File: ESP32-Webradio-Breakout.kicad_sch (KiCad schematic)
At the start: 6 parts

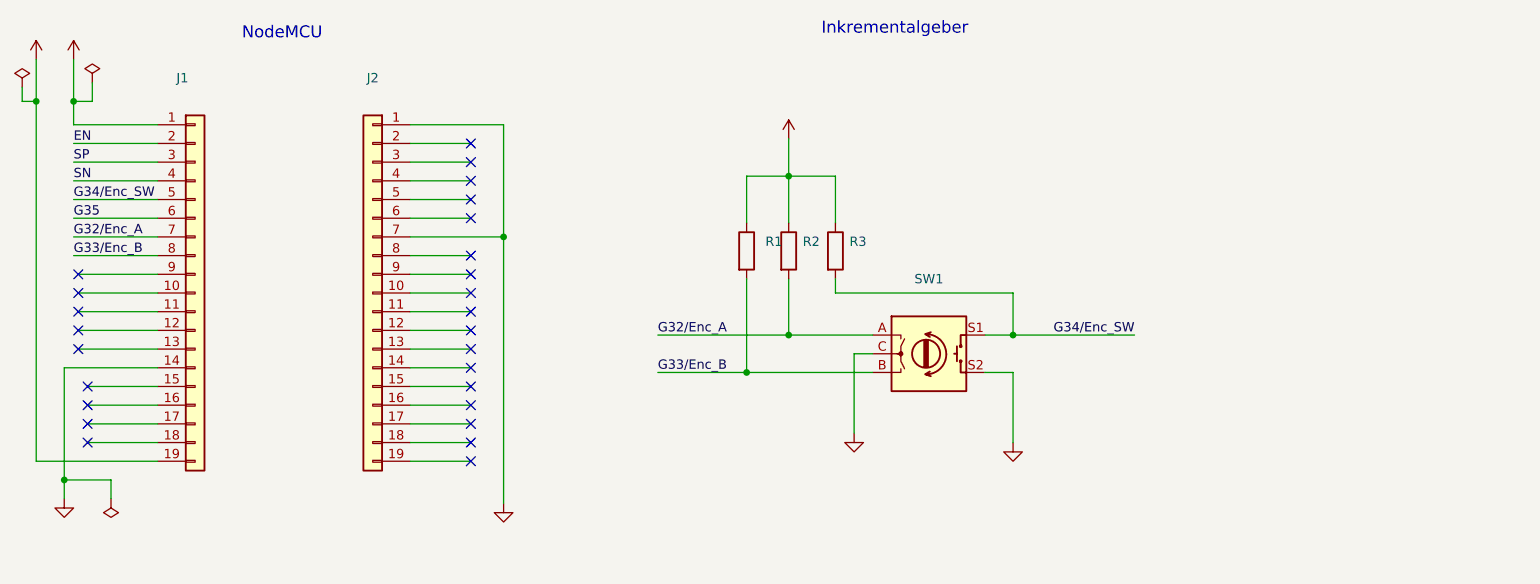
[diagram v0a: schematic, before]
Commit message: adding RCA Jack Connector to board
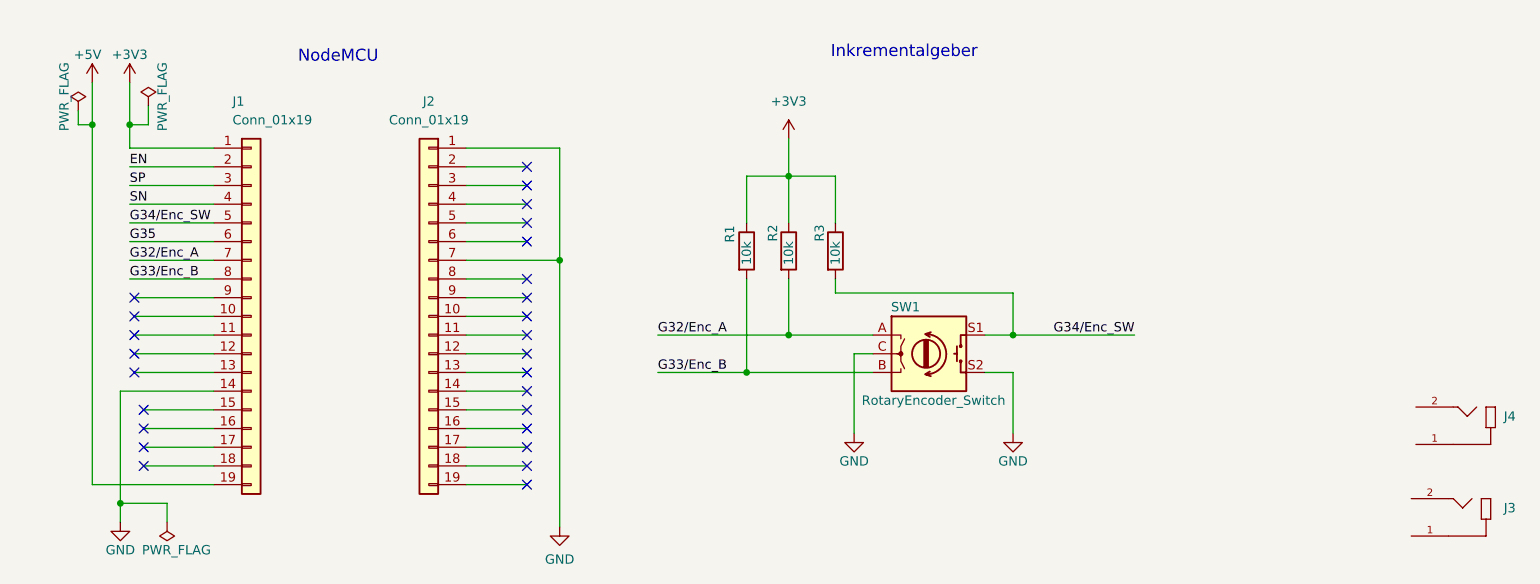
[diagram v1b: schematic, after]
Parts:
- added J3: (no value), symbol RCJ-042:RCJ-042
- added J4: (no value), symbol RCJ-041:RCJ-041
- J1, J2: value (none) -> Conn_01x19; footprint (none) -> Connector_PinSocket_2.54mm:PinSocket_1x19_P2.54mm_Vertical
- R1, R2, R3: value (none) -> 10k; footprint (none) -> Resistor_THT:R_Axial_DIN0207_L6.3mm_D2.5mm_P10.16mm_Horizontal
- SW1: value (none) -> RotaryEncoder_Switch; footprint (none) -> Rotary_Encoder:RotaryEncoder_Alps_EC11E-Switch_Vertical_H20mm
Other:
- moved on the sheet: J1, J2

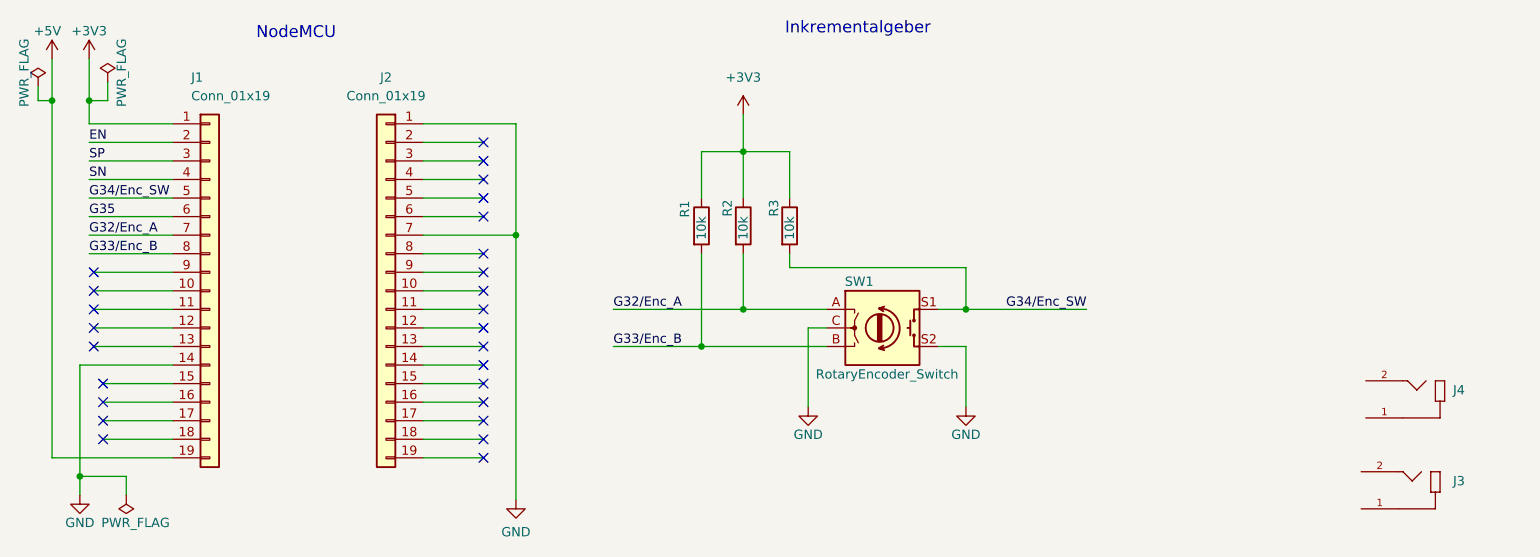
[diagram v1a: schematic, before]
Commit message: adding ESP32-NodeMCU to Project Lib
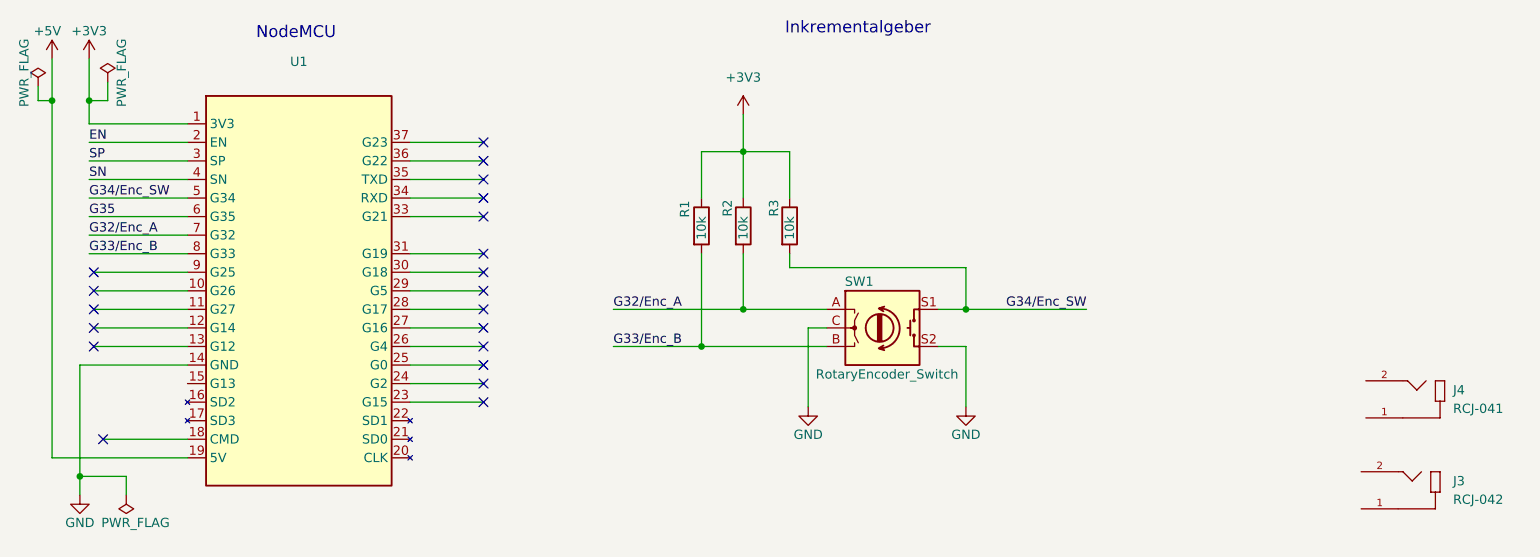
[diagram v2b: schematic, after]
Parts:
- removed J1, J2: Conn_01x19, Connector_PinSocket_2.54mm:PinSocket_1x19_P2.54mm_Vertical, symbol Connector_Generic:Conn_01x19
- added U1: (no value), ESP32-NodeMCU_WROOM_32:ESP32-NodeMCU_WROOM_32, symbol ESP32-NodeMCU_WROOM_32:ESP32NodeMCU
- J3: value (none) -> RCJ-042; footprint (none) -> RCJ-042:CUI_RCJ-042
- J4: value (none) -> RCJ-041; footprint (none) -> RCJ-041:CUI_RCJ-041
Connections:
- net +3V3: now also U1.1 (3V3)
- net +5V: now also U1.19 (5V)
- net EN: now also U1.2 (EN)
- net G32/Enc_A: now also U1.7 (G32)
- net G33/Enc_B: now also U1.8 (G33)
- net G34/Enc_SW: now also U1.5 (G34)
- net G35: now also U1.6 (G35)
- net GND: now also U1.14 (GND)
- net SN: now also U1.4 (SN)
- net SP: now also U1.3 (SP)
- no-connect marks 26 -> 20

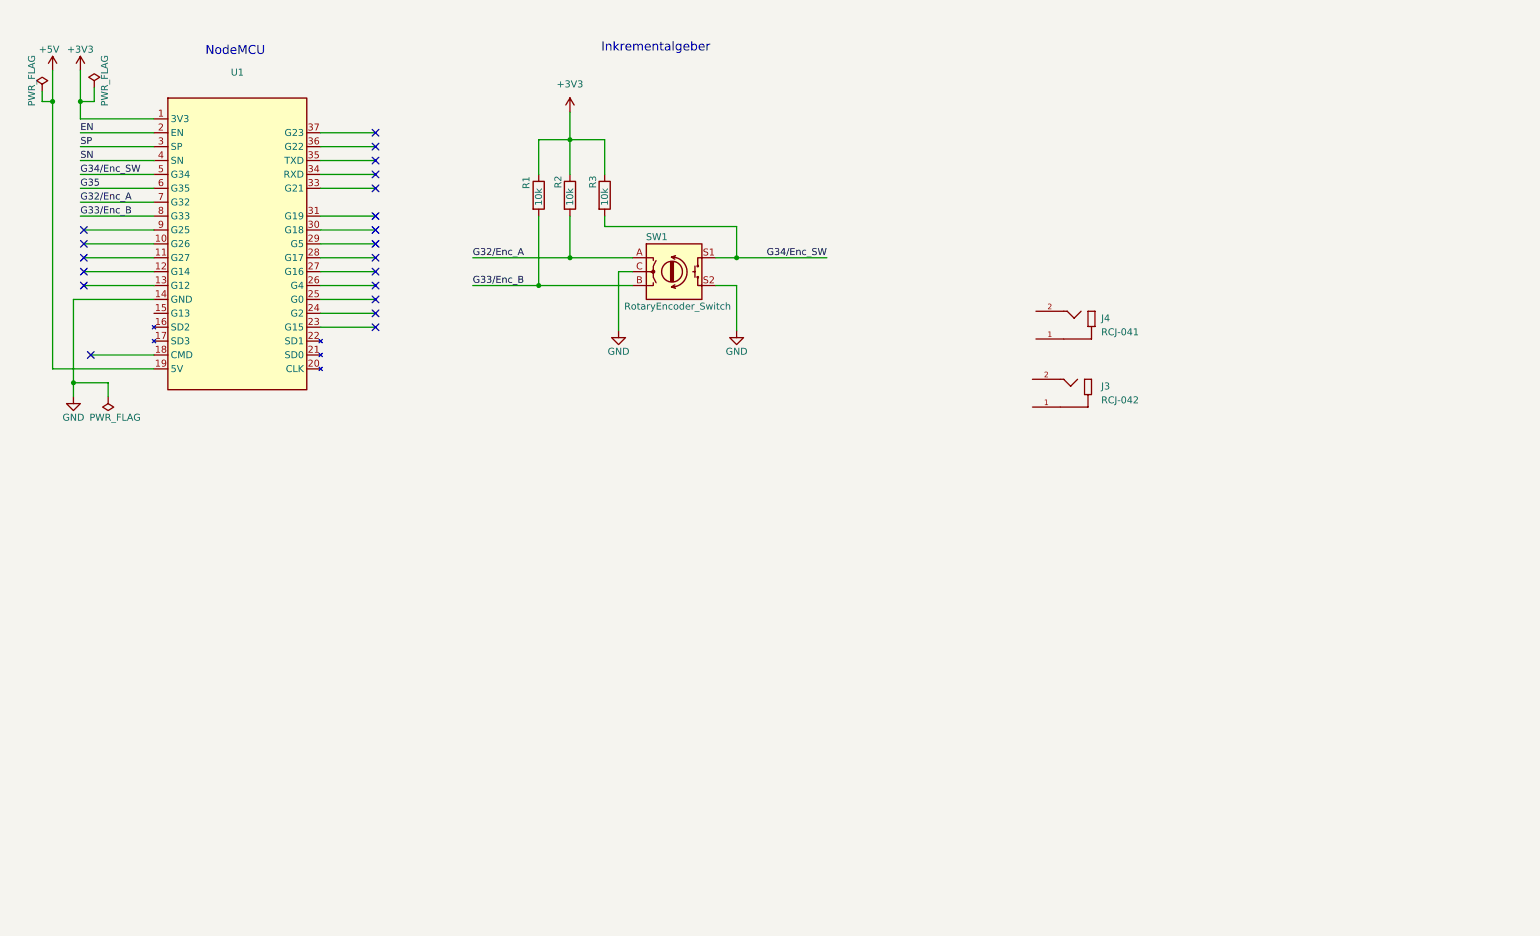
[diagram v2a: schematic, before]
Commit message: adding CC BY-SA 4.0 licens to the Project
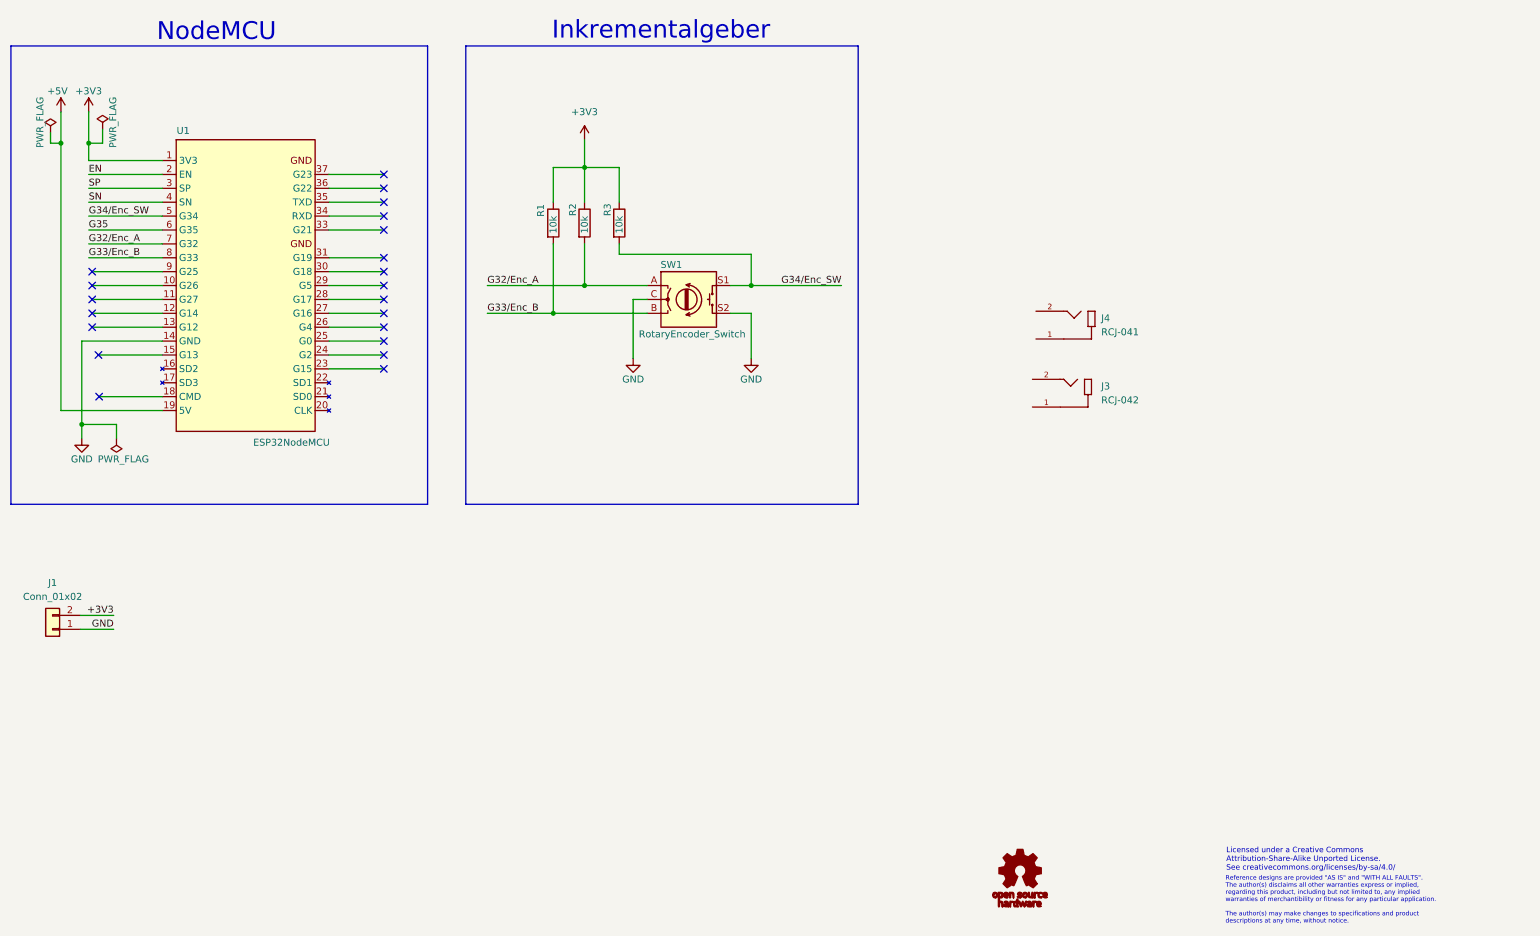
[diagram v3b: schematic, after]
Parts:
- added J1: Conn_01x02, TerminalBlock_RND:TerminalBlock_RND_205-00287_1x02_P5.08mm_Horizontal, symbol Connector_Generic:Conn_01x02
- U1: value (none) -> ESP32NodeMCU
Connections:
- net +3V3: now also J1.2 (Pin_2)
- net GND: now also U1.32 (GND), U1.38 (GND), J1.1 (Pin_1)
- no-connect marks 20 -> 21
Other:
- note added: "Licensed under a Creative Commons Attribution-Share-Alike Unported License. See creativecommons.org/licenses/by-sa/4.0/"
- note added: "Reference designs are provided "AS IS" and "WITH ALL FAULTS". The author(s) disclaims all other warranties express or implied, regarding this product, including but not limited to, any implied warranties of merchantibility or fitness for any particular application. The author(s) may make changes to specifications and product descriptions at any time, without notice."
- company: (none) -> © 2022 - 2023 LUG-Saar e.V., All rights reversed. 
- title: (none) -> ESP32-Webradio-Breakout
- moved on the sheet: R1, R2, R3, SW1

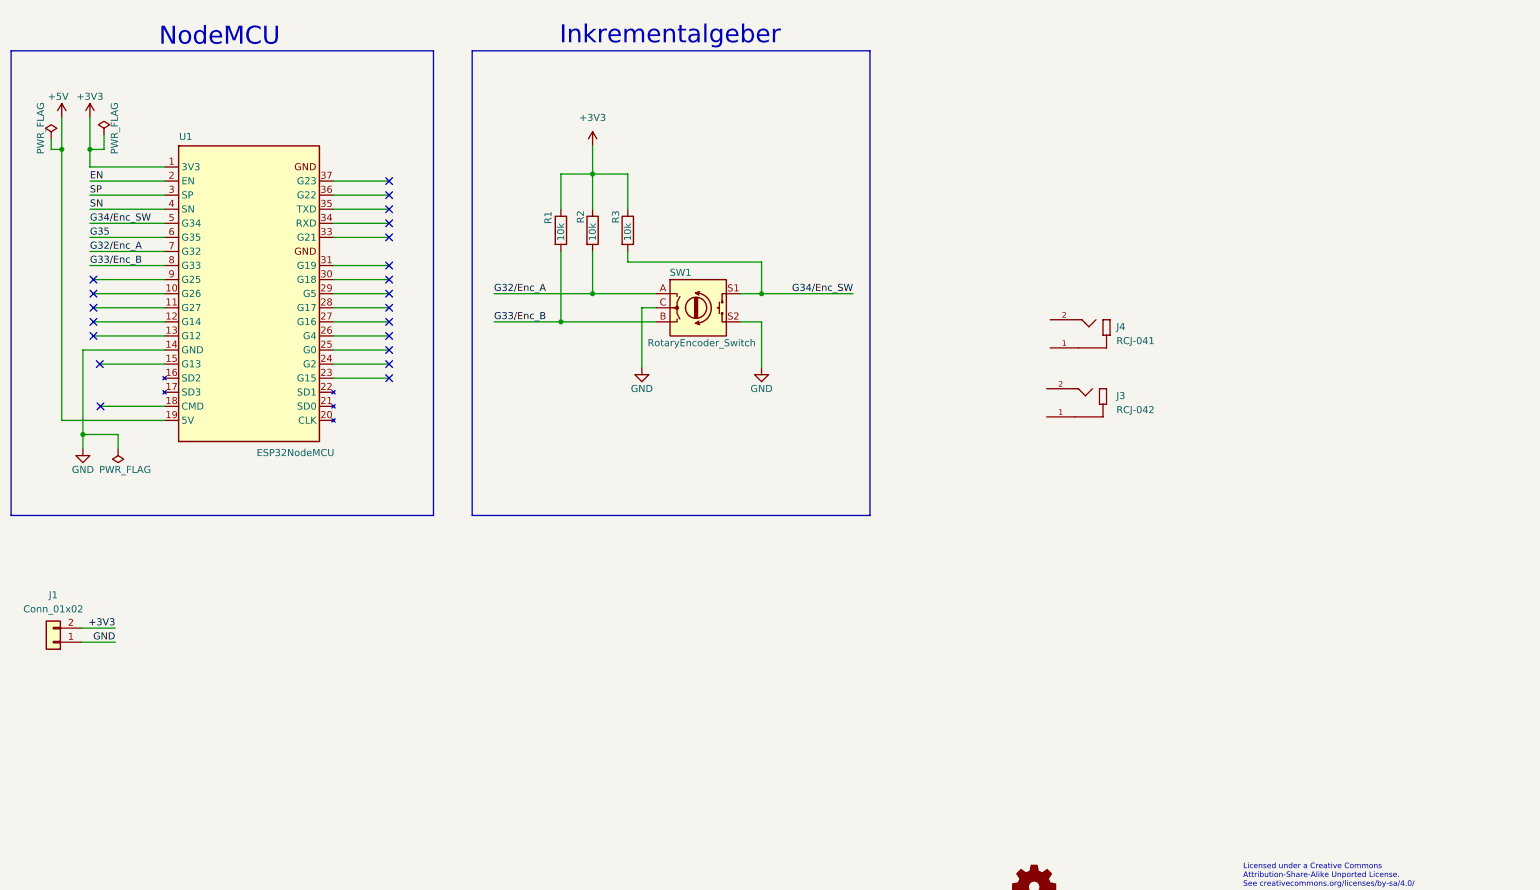
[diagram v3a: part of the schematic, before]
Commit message: adding some Power Supply components
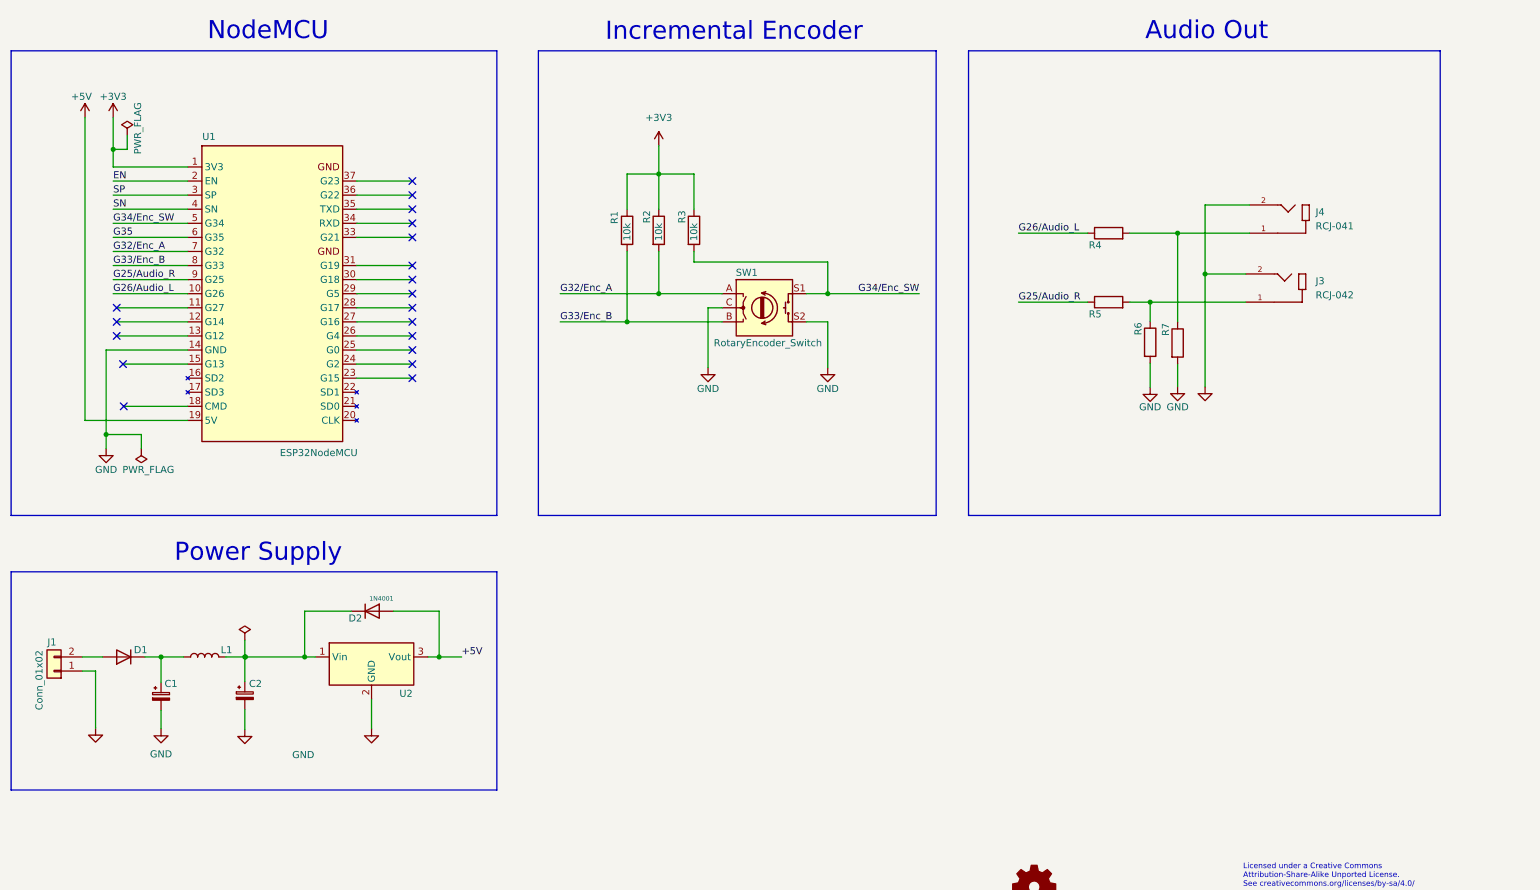
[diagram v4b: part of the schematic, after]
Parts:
- added C1, C2: (no value), symbol Device:C_Polarized_Small
- added D1: (no value), symbol Diode:1N4001
- added D2: 1N4001, Diode_THT:D_DO-41_SOD81_P10.16mm_Horizontal, symbol Diode:1N4001
- added L1: (no value), symbol Device:L
- added R4, R5, R6, R7: (no value), Resistor_THT:R_Axial_DIN0207_L6.3mm_D2.5mm_P10.16mm_Horizontal, symbol Device:R
- added U2: (no value), symbol Regulator_Switching:TSR_1-2450
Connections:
- net +3V3: no longer J1.2 (Pin_2)
- net +5V: now also D2.2 (A), U2.3 (Vout)
- net GND: now also J3.2, J4.2, C1.2, C2.2, R6.2, R7.2, U2.2 (GND)
- net G26/Audio_L: now reaches U1.10 (G26)
- net G26/Audio_L: now also R4.1
- net G25/Audio_R: now reaches U1.9 (G25)
- net G25/Audio_R: now also R5.1
- net at J4.1: now also R4.2, R7.1
- net at J3.1: now also R5.2, R6.1
- new net: C2.1, D2.1 (K), L1.2, U2.1 (Vin)
- new net: C1.1, D1.1 (K), L1.1
- new net: D1.2 (A), J1.2 (Pin_2)
- no-connect marks 21 -> 19
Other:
- note added: "Audio Out"
- note added: "Incremental Encoder"
- note added: "Power Supply"
- note removed: "Inkrementalgeber"
- moved on the sheet: J1, J3, J4, R1, R2, R3, SW1, U1
